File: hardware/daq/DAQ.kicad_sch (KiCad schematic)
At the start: 179 parts, among them J1 ICD15S13E4GX00LF, J2 ICD15S13E4GX00LF, J4 ICD15S13E4GX00LF, J5 ICD15S13E4GX00LF, P1 0022272021, U1 ADS124S08IRHBT, U11 SN74AHCT125RGYR, U2 ADS124S08IRHBT, U3 LT6654BMPS6-5-TRMPBF, U4 LM1086IS-5.0_NOPB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

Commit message: I don't think I did anything lowkey
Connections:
- net FMFV is gone; now on net FMV: D9.4
- net OMFV is gone; now on net OMV: D10.1
- no-connect marks 29 -> 30
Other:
- moved on the sheet: J1, J2, J4, J5

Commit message: starting to clear ERCs, next will try to fit a third RTD
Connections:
- no-connect marks 30 -> 34
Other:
- note added: "DSUB CONNECTORS"
- note removed: "CONNECTORS"
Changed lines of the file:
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@@
 	)
 	(rectangle
-		(start 453.39 135.89)
+		(start 455.93 135.89)
 		(end 576.58 314.96)
 		(stroke
@@
 		)
 	)
-	(text "CONNECTORS"
+	(text "DSUB CONNECTORS"
 		(exclude_from_sim no)
-		(at 260.604 323.088 0)
+		(at 264.16 323.088 0)
 		(effects
 			(font
@@
 	)
 	(junction
+		(at 439.42 163.83)
+		(diameter 0)
+		(color 0 0 0 0)
+	)
+	(junction
 		(at 151.13 290.83)
 		(diameter 0)
@@
 	)
 	(no_connect
+		(at 452.12 351.79)
+	)
+	(no_connect
 		(at 530.86 95.25)
 	)
 	(no_connect
+		(at 157.48 298.45)
+	)
+	(no_connect
 		(at 530.86 59.69)
 	)
@@
 	)
 	(no_connect
+		(at 416.56 359.41)
+	)
+	(no_connect
 		(at 523.24 227.33)
 	)
@@
 	)
 	(no_connect
+		(at 157.48 295.91)
+	)
+	(no_connect
 		(at 523.24 167.64)
 	)
@@
 	(wire
 		(pts
+			(xy 440.69 163.83) (xy 439.42 163.83)
+		)
+		(stroke
+			(width 0)
+			(type default)
+		)
+	)
+	(wire
+		(pts
 			(xy 350.52 74.93) (xy 347.98 74.93)
 		)
@@
 	(wire
 		(pts
-			(xy 436.88 163.83) (xy 438.15 163.83)
+			(xy 436.88 163.83) (xy 439.42 163.83)
 		)
 		(stroke
@@
 	(wire
 		(pts
+			(xy 439.42 162.56) (xy 439.42 163.83)
+		)
+		(stroke
+			(width 0)
+			(type default)
+		)
+	)
+	(wire
+		(pts
 			(xy 151.13 290.83) (xy 157.48 290.83)
 		)
@@
 	)
 	(symbol
+		(lib_id "power:PWR_FLAG")
+		(at 440.69 163.83 270)
+		(unit 1)
+		(exclude_from_sim no)
+		(in_bom yes)
+		(on_board yes)
+		(dnp no)
+		(fields_autoplaced yes)
+		(property "Reference" "#FLG01"
+			(at 442.595 163.83 0)
+			(effects
+				(font
+					(size 1.27 1.27)
+				)
+				(hide yes)
+			)
+		)
+		(property "Value" "PWR_FLAG"
+			(at 444.5 163.8299 90)
+			(effects
+				(font
+					(size 1.27 1.27)
+				)
+				(justify left)
+			)
+		)
+		(property "Footprint" ""
+			(at 440.69 163.83 0)
+			(effects
+				(font
+					(size 1.27 1.27)
+				)
+				(hide yes)
+			)
+		)
+		(property "Datasheet" "~"
+			(at 440.69 163.83 0)
+			(effects
+				(font
+					(size 1.27 1.27)
+				)
+				(hide yes)
+			)
+		)
+		(property "Description" "Special symbol for telling ERC where power comes from"
+			(at 440.69 163.83 0)
+			(effects
+				(font
+					(size 1.27 1.27)
+				)
+				(hide yes)
+			)
+		)
+		(pin "1"
+		)
+		(instances
+			(project ""
+				(path "/98ce85a8-ddff-4ecb-9668-dd271ba07a43"
+					(reference "#FLG01")
+					(unit 1)
+				)
+			)
+		)
+	)
+	(symbol
 		(lib_id "Device:C")
 		(at 78.74 167.64 0)
@@
 	(symbol
 		(lib_id "power:+5V")
-		(at 438.15 163.83 0)
+		(at 439.42 162.56 0)
 		(unit 1)
 		(exclude_from_sim no)
@@
 		(dnp no)
 		(property "Reference" "#PWR096"
-			(at 438.15 167.64 0)
+			(at 439.42 166.37 0)
 			(effects
 				(font
@@
 		)
 		(property "Value" "5V REF"
-			(at 437.896 160.02 0)
+			(at 439.166 158.75 0)
 			(effects
 				(font
@@
 		)
 		(property "Footprint" ""
-			(at 438.15 163.83 0)
+			(at 439.42 162.56 0)
 			(effects
 				(font
@@
 		)
 		(property "Datasheet" ""
-			(at 438.15 163.83 0)
+			(at 439.42 162.56 0)
 			(effects
 				(font
@@
 		)
 		(property "Description" "Power symbol creates a global label with name \"+5V\""
-			(at 438.15 163.83 0)
+			(at 439.42 162.56 0)
 			(effects
 				(font

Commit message: added 3rd RTD to ADC3 and added some PWR FLAGs for ERCs
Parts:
- removed C79, C81, C82: 16nF, GRM3195C2A163JA01D:CAPC3216X95N, symbol Device:C
- removed R43, R49, R50: 10k, Resistor_SMD:R_0603_1608Metric, symbol Device:R
- added C85, C86: 3.3nF, footprintsCL10:CAP_CL10_SAM, symbol Device:C
- added C96, C97, C98, C99: 16nF, GRM3195C2A163JA01D:CAPC3216X95N, symbol Device:C
- added R56: 5.6k, Resistor_SMD:R_0603_1608Metric, symbol Device:R
- added R57: 1.8k, Resistor_SMD:R_0603_1608Metric, symbol Device:R
- added R58, R59, R60, R61: 10k, Resistor_SMD:R_0603_1608Metric, symbol Device:R
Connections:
- net GND: now also C96.2, C97.2, C98.2, C99.2, R57.2
- net PT10_SIG: now also R48.1; no longer R45.1
- net PT11_SIG: now also R44.1; no longer R46.1
- net PT12_SIG: now also R55.1; no longer R47.1
- net PT1_SIG: now also J4.12; no longer J1.4
- net PT2_SIG: now also J4.13; no longer J1.6
- net PT3_SIG: now also J4.14; no longer J1.14
- net PT7_SIG: now also R45.1
- net PT8_SIG: now also R46.1
- net PT9_SIG: now also R47.1
- net IDAC2_3: now reaches U9.4 (AIN3)
- net IDAC2_3: now also D9.1, J1.6, R61.2
- net IDAC1_3: now reaches U9.2 (AIN5)
- net IDAC1_3: now also R56.1, R58.2
- net at U9.5 (AIN2): now also C86.2, C98.1, R61.1
- net at U9.3 (AIN4): now also C86.1, C97.1, R60.1
- net at U9.31 (REFN1_AIN7): now also C85.1, C96.1, R58.1
- net at U9.32 (REFP1_AIN6): now also C85.2, C99.1, R59.1
- removed net PT13_SIG: D4.4, J4.12, R48.1
- removed net PT14_SIG: D5.6, J4.13, R44.1
- removed net PT15_SIG: D9.3, J4.14, R55.1
- new net RTD3_L1: D4.4, J1.4, R56.2, R59.2, R60.2
- new net RTD3_L3: D9.3, J1.14, R57.1
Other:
- note added: "RTDs"
- note added: "TOTAL SENSOR CAPABILITIES: - 12 PTs (3- or 4-wire) - 3 RTDs (3-wire) - 3 Load Cells (2x 5V, 1x 10V Excitement)"
- note removed: "RTDs & PTs"
- note removed: "TOTAL SENSOR CAPABILITIES: - 15 PTs - 2 RTDs - 3 Load Cells"
- moved on the sheet: C1, C10, C11, C17, C18, C2, C24, C25, C3, C30, C31, C34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

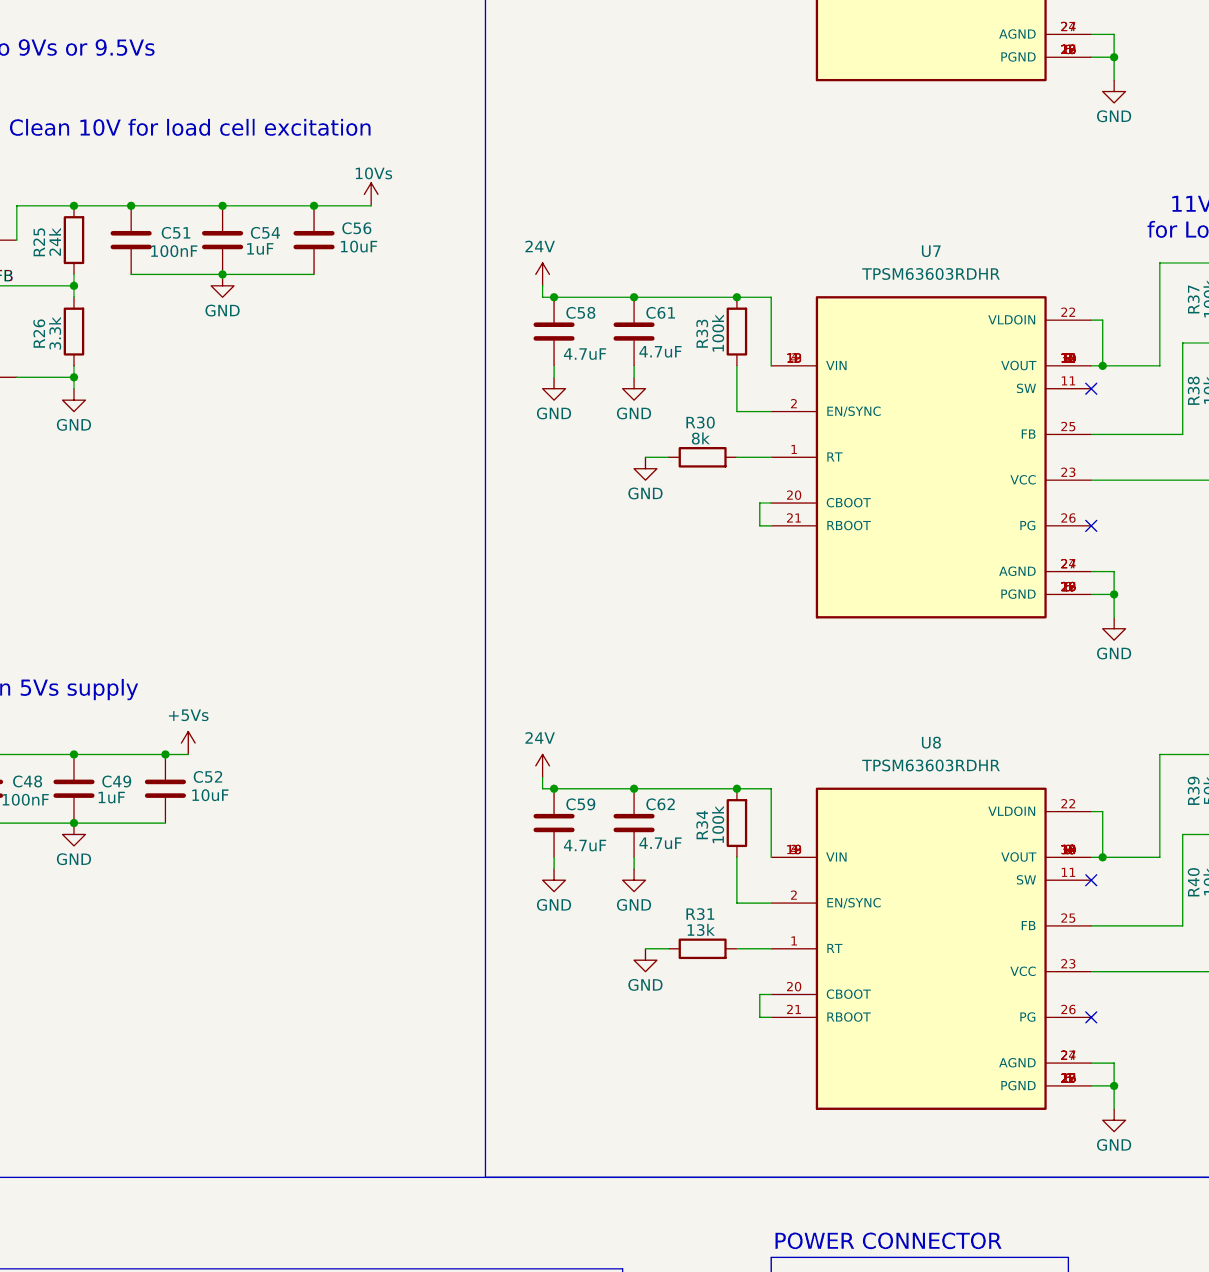
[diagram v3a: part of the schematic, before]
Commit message: changed stackup to 4 copper layers
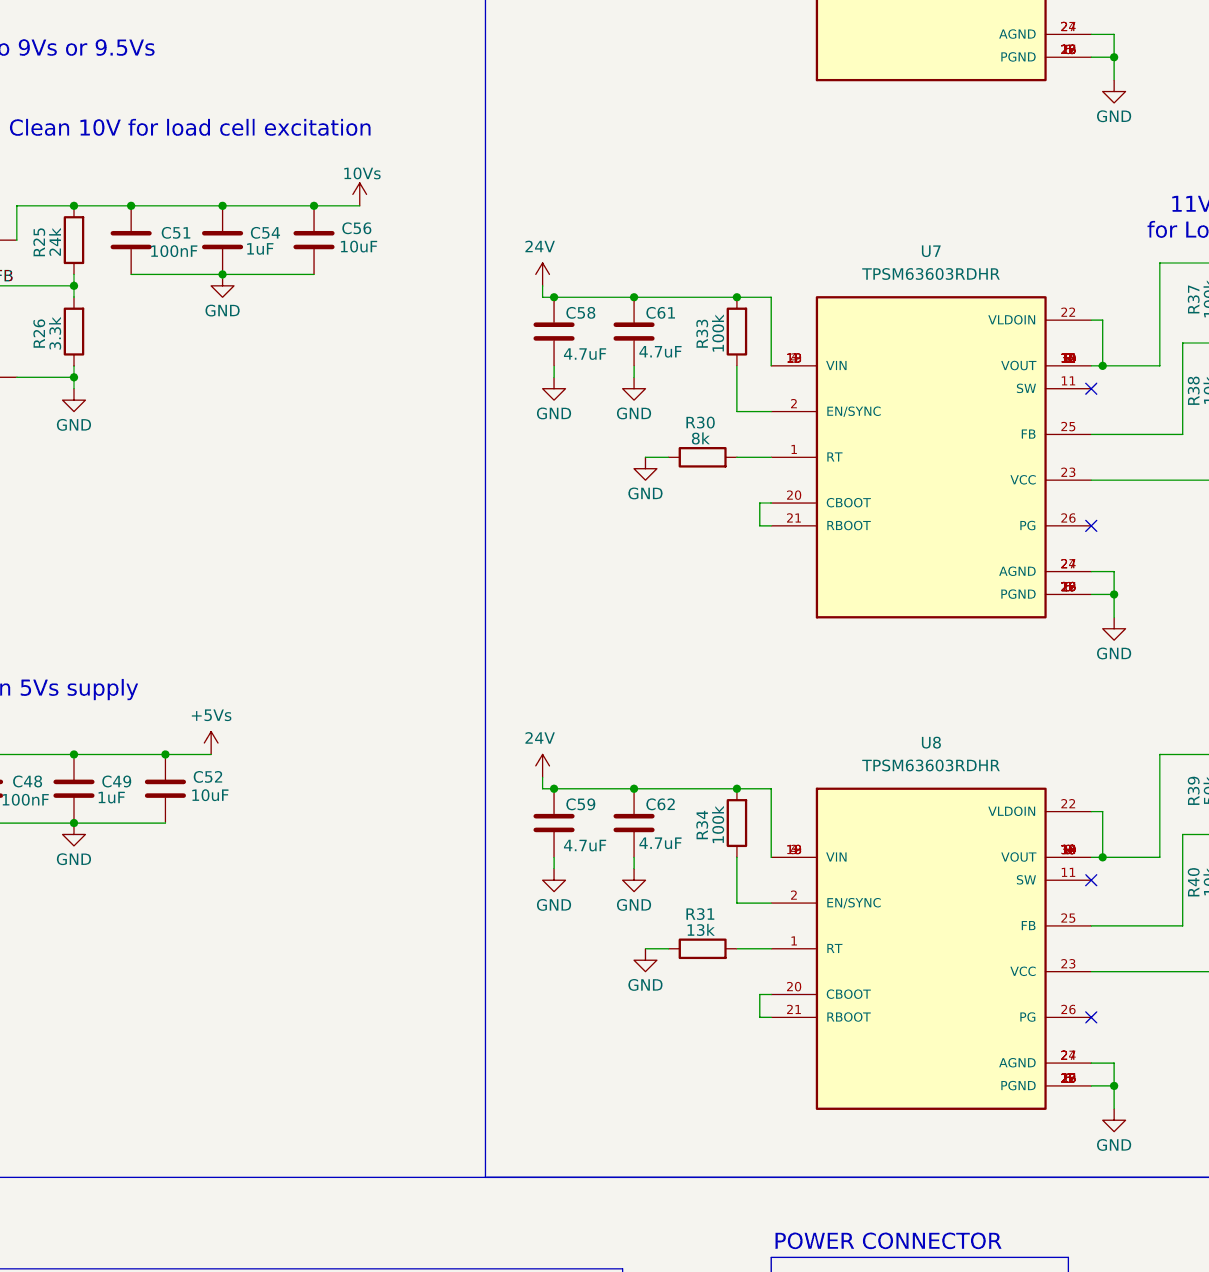
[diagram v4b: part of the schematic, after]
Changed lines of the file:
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@@
 	(wire
 		(pts
+			(xy 436.88 207.01) (xy 441.96 207.01)
+		)
+		(stroke
+			(width 0)
+			(type default)
+		)
+	)
+	(wire
+		(pts
 			(xy 364.49 64.77) (xy 374.65 64.77)
 		)
@@
 	(wire
 		(pts
-			(xy 420.37 267.97) (xy 422.91 267.97)
+			(xy 420.37 267.97) (xy 425.45 267.97)
 		)
 		(stroke
@@
 	(wire
 		(pts
-			(xy 443.23 207.01) (xy 436.88 207.01)
-		)
-		(stroke
-			(width 0)
-			(type default)
-		)
-	)
-	(wire
-		(pts
 			(xy 140.97 55.88) (xy 148.59 55.88)
 		)
@@
 	(symbol
 		(lib_id "power:+5V")
-		(at 422.91 267.97 0)
+		(at 425.45 267.97 0)
 		(unit 1)
 		(exclude_from_sim no)
@@
 		(dnp no)
 		(property "Reference" "#PWR092"
-			(at 422.91 271.78 0)
+			(at 425.45 271.78 0)
 			(effects
 				(font
@@
 		)
 		(property "Value" "+5Vs"
-			(at 422.91 263.652 0)
+			(at 425.45 263.652 0)
 			(effects
 				(font
@@
 		)
 		(property "Footprint" ""
-			(at 422.91 267.97 0)
+			(at 425.45 267.97 0)
 			(effects
 				(font
@@
 		)
 		(property "Datasheet" ""
-			(at 422.91 267.97 0)
+			(at 425.45 267.97 0)
 			(effects
 				(font
@@
 		)
 		(property "Description" "Power symbol creates a global label with name \"+5V\""
-			(at 422.91 267.97 0)
+			(at 425.45 267.97 0)
 			(effects
 				(font
@@
 	(symbol
 		(lib_id "power:+9V")
-		(at 443.23 207.01 0)
+		(at 441.96 207.01 0)
 		(unit 1)
 		(exclude_from_sim no)
@@
 		(dnp no)
 		(property "Reference" "#PWR097"
-			(at 443.23 210.82 0)
+			(at 441.96 210.82 0)
 			(effects
 				(font
@@
 		)
 		(property "Value" "10Vs"
-			(at 443.484 203.454 0)
+			(at 442.214 203.454 0)
 			(effects
 				(font
@@
 		)
 		(property "Footprint" ""
-			(at 443.23 207.01 0)
+			(at 441.96 207.01 0)
 			(effects
 				(font
@@
 		)
 		(property "Datasheet" ""
-			(at 443.23 207.01 0)
+			(at 441.96 207.01 0)
 			(effects
 				(font
@@
 		)
 		(property "Description" "Power symbol creates a global label with name \"+9V\""
-			(at 443.23 207.01 0)
+			(at 441.96 207.01 0)
 			(effects
 				(font
